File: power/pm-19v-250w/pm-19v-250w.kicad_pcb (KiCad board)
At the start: 4 copper layers, 58.4 x 22.9 mm, 57 parts, among them J1 Screw pads S1-S4, J2 Aux pads 2x3, Q1 BSC070N10NS5, Q2 BSC070N10NS5, Q3 BSC070N10NS5, Q4 BSC070N10NS5, U1 LTC7810, U2 MCP65R46-1.21, U3 MCP65R46-1.21

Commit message: pm-19v-250w: silk (pcbkit silk) + tools/silk_labels.py: J1 ref hidden, screw net labels VIN/GND/GND/VOUT on both sides (B VOUT: no room), J2 ref on B by its pads; silk DRC 105 -> 2 (both footprint-internal)
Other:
- board text added: "GND"
- board text added: "J2"
- board text added: "VIN"
- board text added: "VOUT"

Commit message: pm-19v-250w: L1/L2 COILANK APS1510M220F (C49261404, JLC stock) on the XAL1510 footprint (terminals match the pads, body inside the courtyard)
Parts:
- L1, L2: value 22u XAL1510-223 -> 22u APS1510M220F
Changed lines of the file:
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@@
 			)
 		)
-		(property "Value" "22u XAL1510-223"
+		(property "Value" "22u APS1510M220F"
 			(at 0 9.15 180)
 			(layer "F.Fab")
@@
 			)
 		)
+		(property "LCSC" "C49261404"
+			(at 0 0 0)
+			(layer "F.Fab")
+			(hide yes)
+			(effects
+				(font
+					(size 1.27 1.27)
+				)
+			)
+		)
 		(sheetname "pm-19v-250w")
 		(sheetfile "pm-19v-250w.kicad_sch")
@@
 			)
 		)
-		(property "Value" "22u XAL1510-223"
+		(property "Value" "22u APS1510M220F"
 			(at 0 9.15 0)
 			(layer "F.Fab")
@@
 				)
 			)
+		)
+		(property "LCSC" "C49261404"
+			(at 0 0 0)
+			(layer "F.Fab")
+			(hide yes)
+			(effects
+				(font
+					(size 1.27 1.27)
+				)
+			)

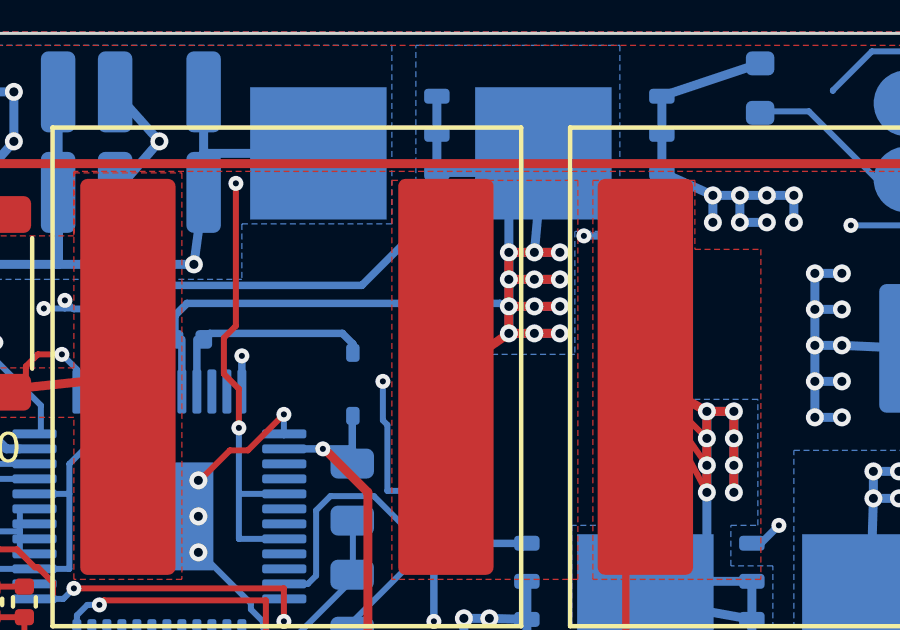
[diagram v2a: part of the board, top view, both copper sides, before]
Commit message: pm-19v-250w: BG2 on B.Cu only, no vias (Q4 gate via sat 0.2 mm from L1's SW1 pad); R1's VIN via down 0.6 mm to clear the lane; route scripts match; DRC unchanged, 0 unconnected
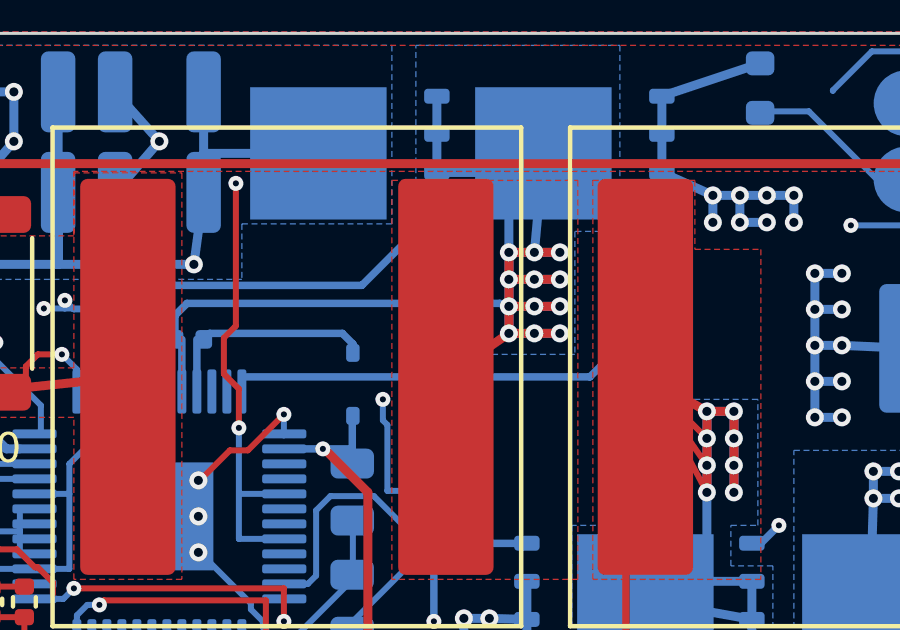
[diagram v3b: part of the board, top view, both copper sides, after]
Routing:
- net /BG2: track 22.0 -> 18.6 mm, vias 2 -> 0

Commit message: PM aux contacts: 2x3 1.27 mm SMT header (module J2, C41376035) into SMT socket (carrier J3, C41397112) replaces flat pads + pogos; standoffs M2 x 7 (C2916355), gap 7.0 mm. pmmount.py generates the new footprints; module J2 swapped in place, tools/route_aux.py moves PGOOD's via and adds a GND via between the columns (DRC as before, 0 unconnected, parity clean); carrier PG1-PG6 -> J3 and rebuilt by its flow (DRC 0 errors, 0 unconnected, parity clean); spec, ADR 0003 (6, 7), power-board.md and handoff updated; ID open = slot fault rule
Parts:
- J2: value Aux pads 2x3 -> Aux header 2x3 1.27; footprint pm:PM_Aux_Pads_2x03 -> pm:PM_Aux_Header_2x03_P1.27; moved to B.Cu
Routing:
- net GND: track 139.2 -> 133.9 mm, vias 48 -> 49
- net /PGOOD: track 10.4 -> 11.6 mm
- net /ID: track 4.85 -> 5.65 mm
